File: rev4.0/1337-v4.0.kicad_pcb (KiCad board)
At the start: 2 copper layers, 62 x 62 mm, 62 parts, among them J1 USB_IN, J2 AVR-ISP-6, SW1 SW_Push, U1 SSD1306, U2 USBLC6-2SC6, U3 ATMEGA32U4, Y1 16MHz

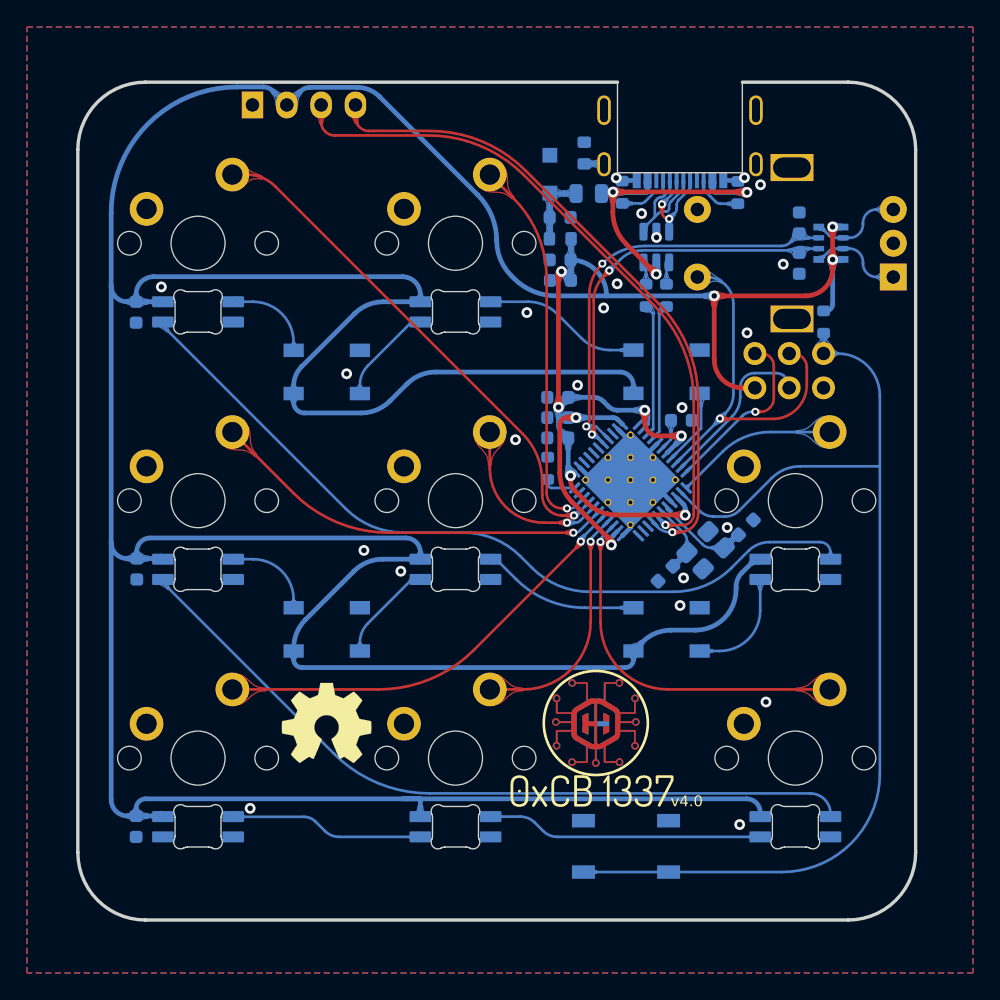
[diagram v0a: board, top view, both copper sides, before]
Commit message: added 3D PCB models
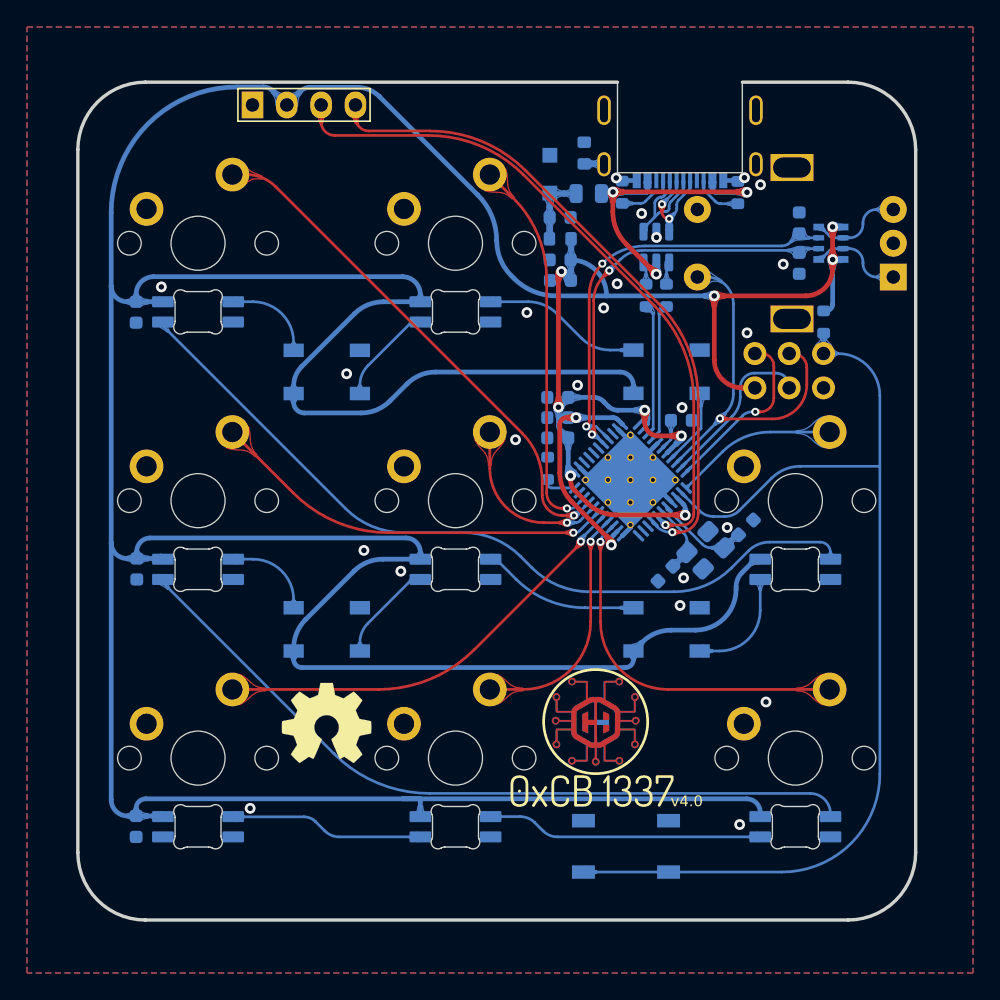
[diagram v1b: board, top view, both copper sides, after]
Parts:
- removed the G*** at (111.8, 81.8)
- added G***: LOGO, art:logo, B.Cu at (111.8, 81.7)

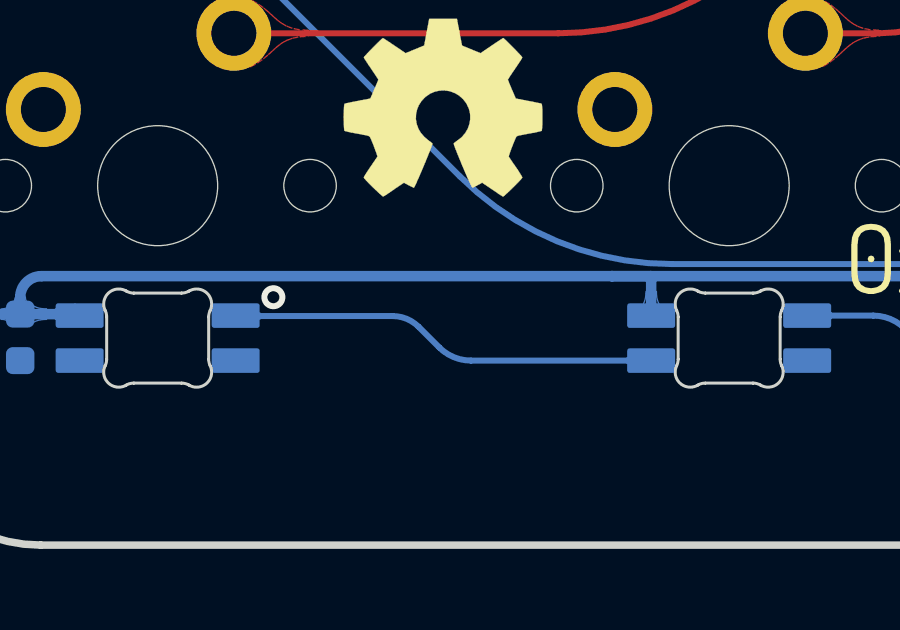
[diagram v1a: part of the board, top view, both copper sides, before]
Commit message: added OSHWA mark and exported prod files
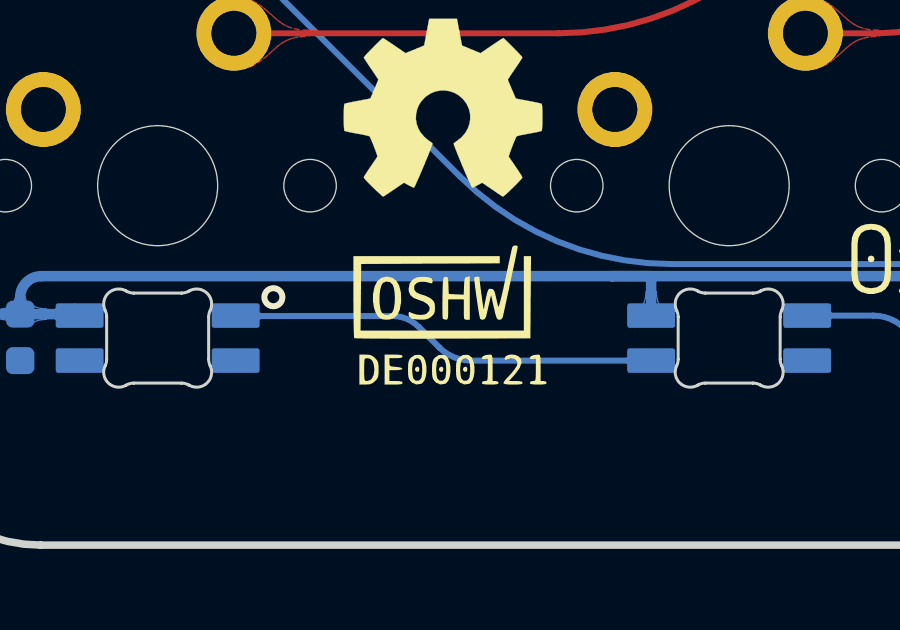
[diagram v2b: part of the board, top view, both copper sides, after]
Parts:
- added G***: OSHWA, art:OSHWA, F.Cu at (91.8, 88.7)
- added G***: OSHWA, art:OSHWA, B.Cu at (91.8, 88.7)
